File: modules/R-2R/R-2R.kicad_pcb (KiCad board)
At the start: 2 copper layers, 40.6 x 40.6 mm, 25 parts, among them J1 Conn_01x10_Male, J2 Conn_01x10_Male, J3 Conn_01x01_Male, U1 74LS573

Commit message: R-2R, polishing
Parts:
- added J4: Conn_01x01_Male, Connector_PinHeader_2.54mm:PinHeader_1x01_P2.54mm_Vertical, F.Cu at (117.5, 54.6)
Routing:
- net GND: track 55.6 -> 65.4 mm
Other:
- board text added: "19e5d0"
- board text added: "Out"
- board text removed: "hash"

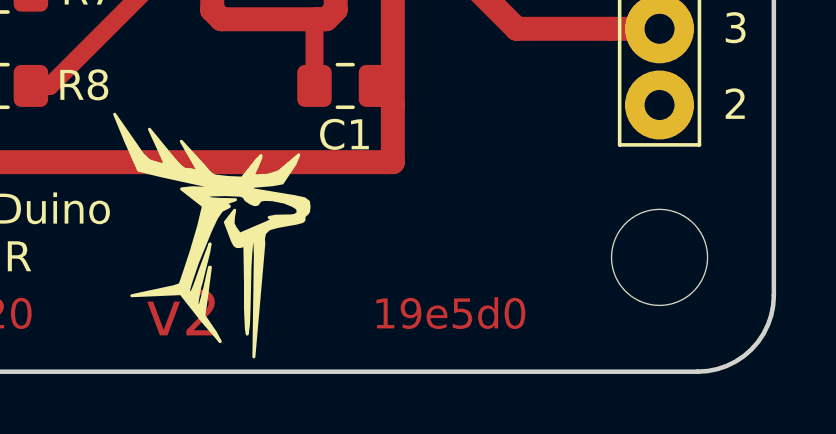
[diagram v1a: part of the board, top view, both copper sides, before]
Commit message: R-2R. Add photomask in pdf.
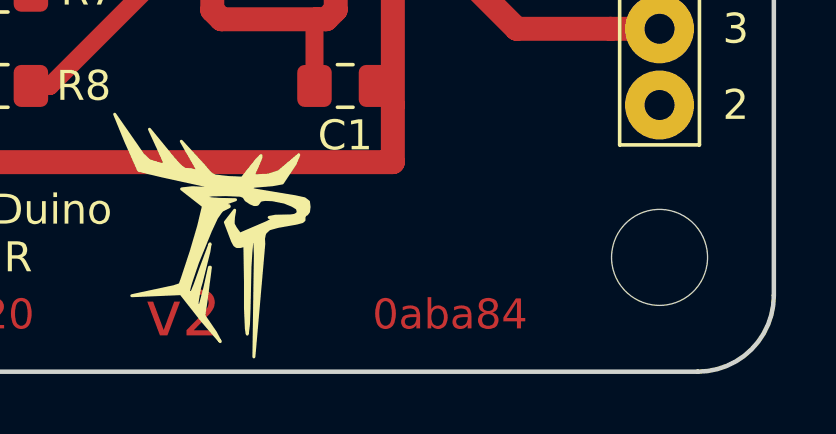
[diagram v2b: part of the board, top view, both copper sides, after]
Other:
- board text added: "0aba84"
- board text removed: "19e5d0"
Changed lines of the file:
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@@
   )
   (setup
-    (last_trace_width 0.8)
+    (last_trace_width 0.25)
     (user_trace_width 0.6)
     (user_trace_width 0.8)
@@
     (effects (font (size 1 1) (thickness 0.15)))
   )
-  (gr_text 19e5d0 (at 118.745 89.535) (layer F.Cu)
+  (gr_text 0aba84 (at 118.745 89.535) (layer F.Cu)
     (effects (font (size 1 1) (thickness 0.2)))
   )

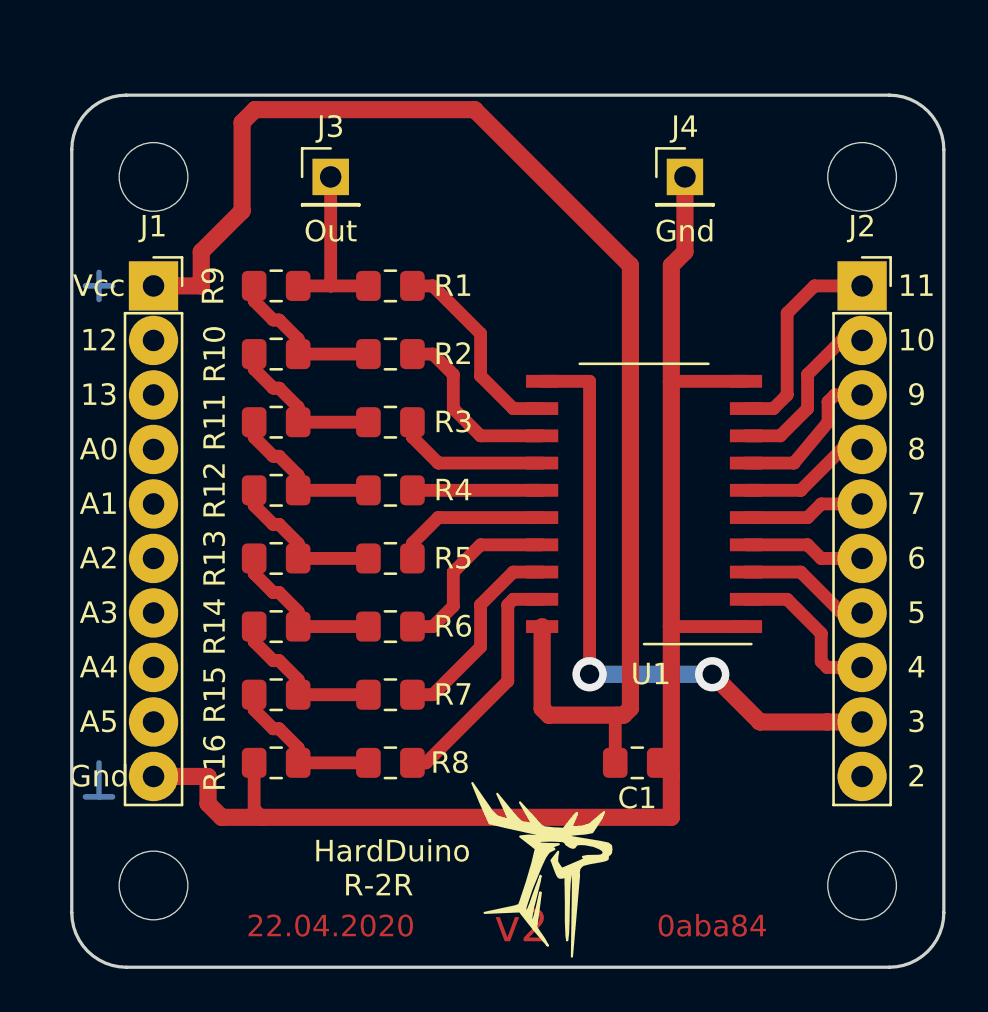
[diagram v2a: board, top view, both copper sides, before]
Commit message: 1x PCBs. Move holes to edges. Caution! This changes is uncompatible with previous versions...
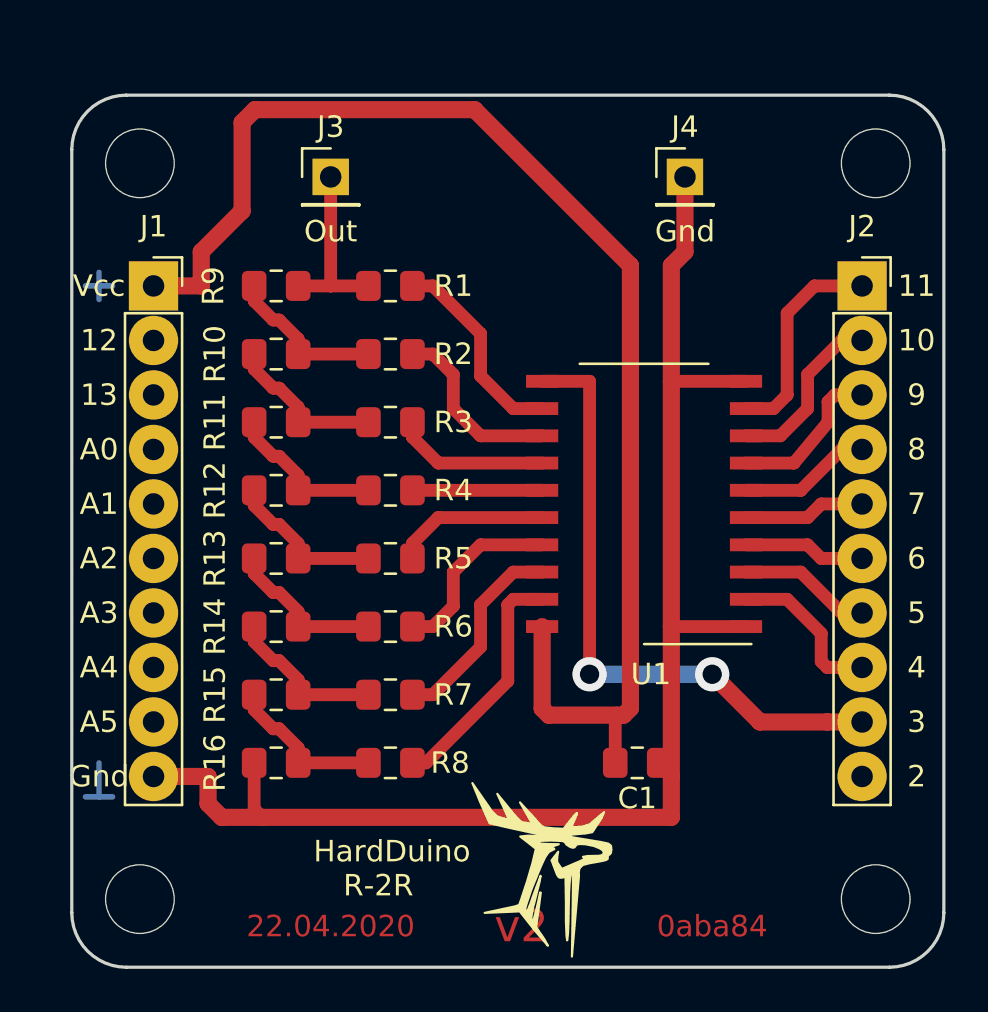
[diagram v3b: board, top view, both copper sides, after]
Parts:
- moved H2 0.90 mm to (92.1, 88.3)
- moved H4 0.90 mm to (126.4, 88.3)
- moved H1 0.90 mm to (92.1, 54.0)
- moved H3 0.90 mm to (126.4, 54.0)
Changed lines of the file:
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@@
   )
   (module MountingHole:MountingHole_3.2mm_M3 (layer F.Cu)
-    (at 92.71 54.61)
+    (at 92.0750 53.9750)
     (descr "Mounting Hole 3.2mm, no annular, M3")
     (tags "mounting hole 3.2mm no annular m3")
@@
   )
   (module MountingHole:MountingHole_3.2mm_M3 (layer F.Cu)
-    (at 92.71 87.63)
+    (at 92.0750 88.2650)
     (descr "Mounting Hole 3.2mm, no annular, M3")
     (tags "mounting hole 3.2mm no annular m3")
@@
   )
   (module MountingHole:MountingHole_3.2mm_M3 (layer F.Cu)
-    (at 125.73 54.61)
+    (at 126.3650 53.9750)
     (descr "Mounting Hole 3.2mm, no annular, M3")
     (tags "mounting hole 3.2mm no annular m3")
@@
   )
   (module MountingHole:MountingHole_3.2mm_M3 (layer F.Cu)
-    (at 125.73 87.63)
+    (at 126.3650 88.2650)
     (descr "Mounting Hole 3.2mm, no annular, M3")
     (tags "mounting hole 3.2mm no annular m3")

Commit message: Fix hash & version
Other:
- board text added: "21.02.2021"
- board text added: "b4d799"
- board text added: "v2.3"
- board text removed: "0aba84"
- board text removed: "22.04.2020"
- board text removed: "v2"

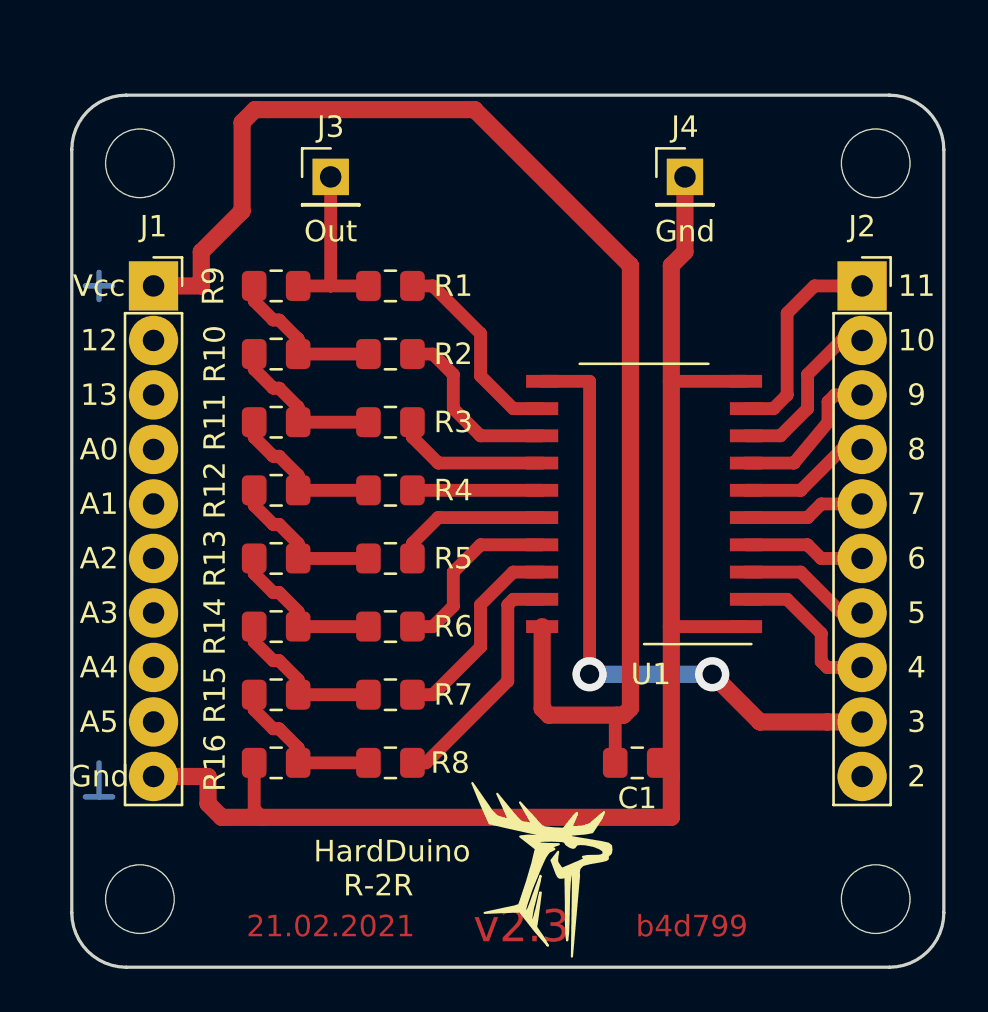
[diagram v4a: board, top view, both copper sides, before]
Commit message: All 1x shields was rotated clockwise
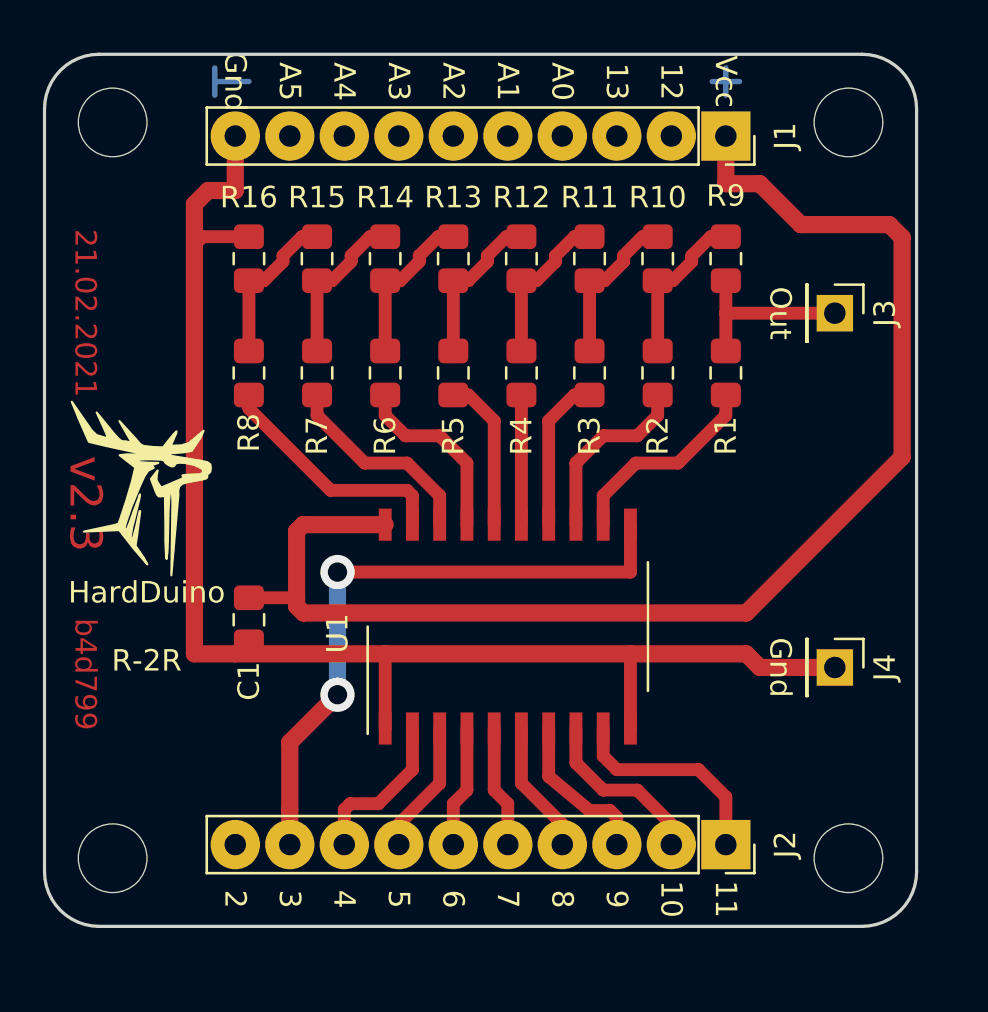
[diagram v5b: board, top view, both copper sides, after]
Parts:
- moved H2 36.2 mm to (90.8, 52.1), turned to 270 degrees
- moved H4 35.6 mm to (90.8, 86.4), turned to 270 degrees
- moved H1 33.1 mm to (125.1, 52.1), turned to 270 degrees
- moved H3 32.4 mm to (125.1, 86.4), turned to 270 degrees
- moved J1 27.6 mm to (119.4, 52.7), turned to 270 degrees
- moved J2 26.8 mm to (119.4, 85.7), turned to 270 degrees
- moved J3 24.3 mm to (124.5, 61.0), turned to 270 degrees
- moved J4 23.9 mm to (124.5, 77.5), turned to 270 degrees
- moved R16 23.5 mm to (97.2, 58.4), turned to 270 degrees
- moved R9 21.0 mm to (119.4, 58.4), turned to 270 degrees
- moved R15 20.4 mm to (100.3, 58.4), turned to 270 degrees
- moved R8 19.3 mm to (97.2, 63.7), turned to 270 degrees
- moved C1 19.3 mm to (97.2, 75.2), turned to 90 degrees
- moved R10 18.3 mm to (116.2, 58.4), turned to 270 degrees
- moved R14 17.9 mm to (103.5, 58.4), turned to 270 degrees
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
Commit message: Now all mounting holes have distance 31.92 x 31.1
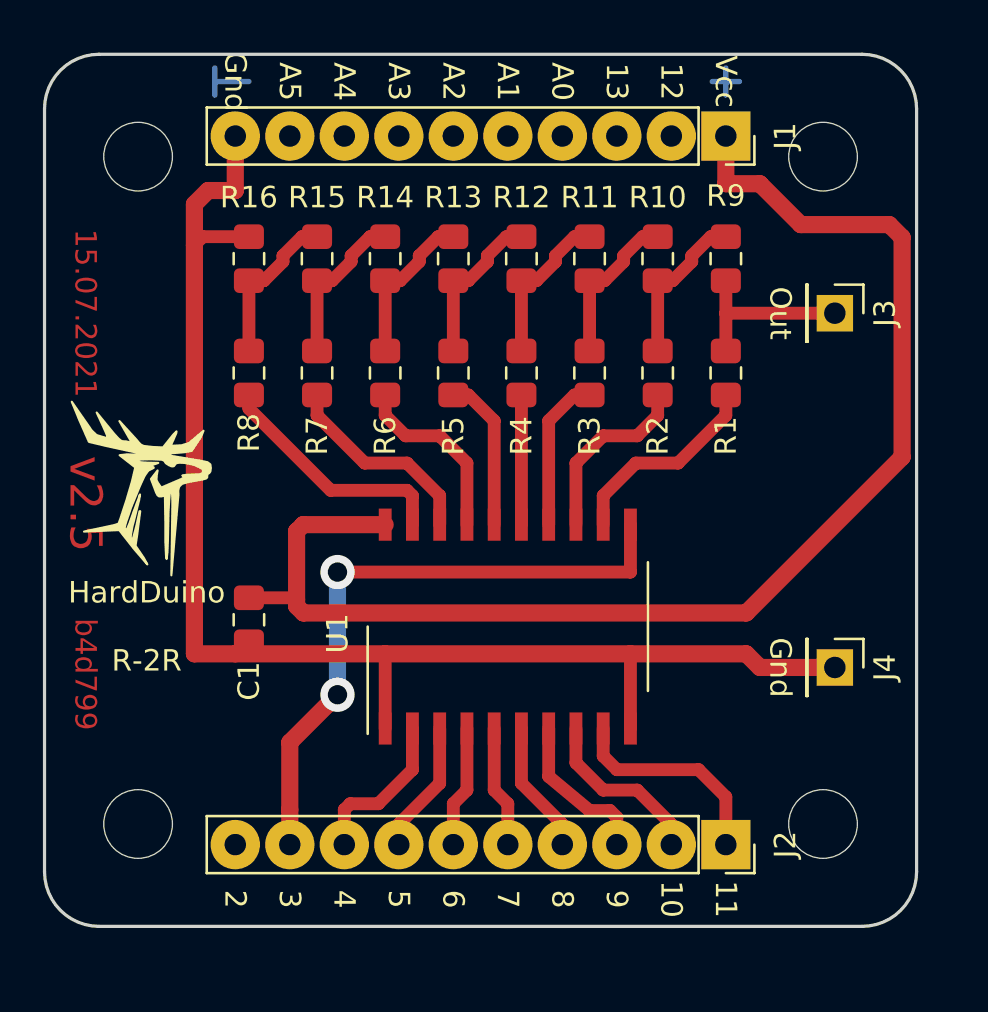
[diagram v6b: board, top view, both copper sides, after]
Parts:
- moved H1 1.99 mm to (123.9, 53.7), turned to 0 degrees
- moved H3 1.99 mm to (123.9, 84.8), turned to 0 degrees
- moved H2 1.99 mm to (92.0, 53.7), turned to 0 degrees
- moved H4 1.99 mm to (92.0, 84.8), turned to 0 degrees
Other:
- board text added: "15.07.2021"
- board text added: "v2.5"
- board text removed: "21.02.2021"
- board text removed: "v2.3"
